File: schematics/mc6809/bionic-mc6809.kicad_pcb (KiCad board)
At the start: 2 copper layers, 48.3 x 71.1 mm, 12 parts, among them J1 Bionic-P135, J1 BionicConnector, J2 Bionic-P245, U1 MC6809P, U2 74HCT126, U3 11AA010-I/TO

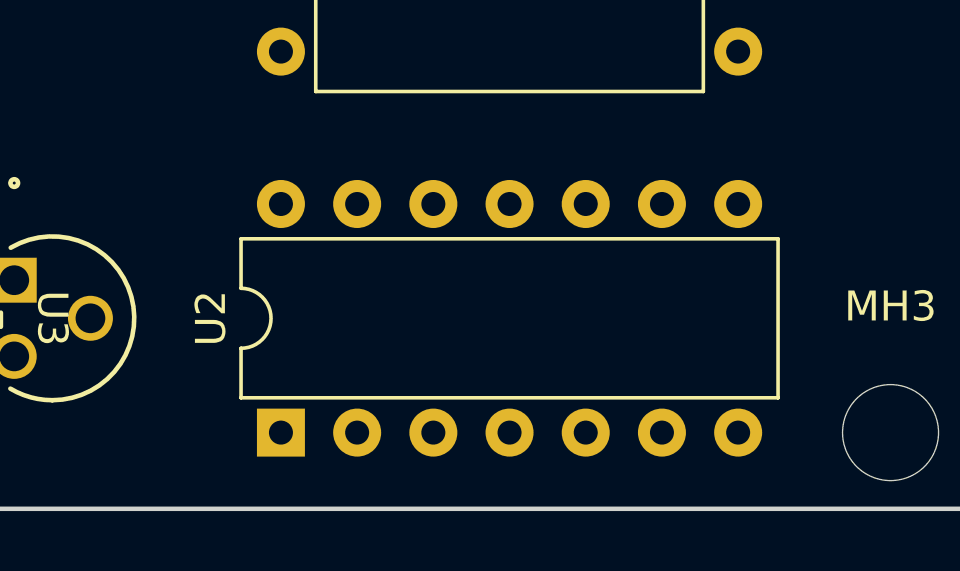
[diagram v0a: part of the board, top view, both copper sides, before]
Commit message: [MC6809] Remove HC126
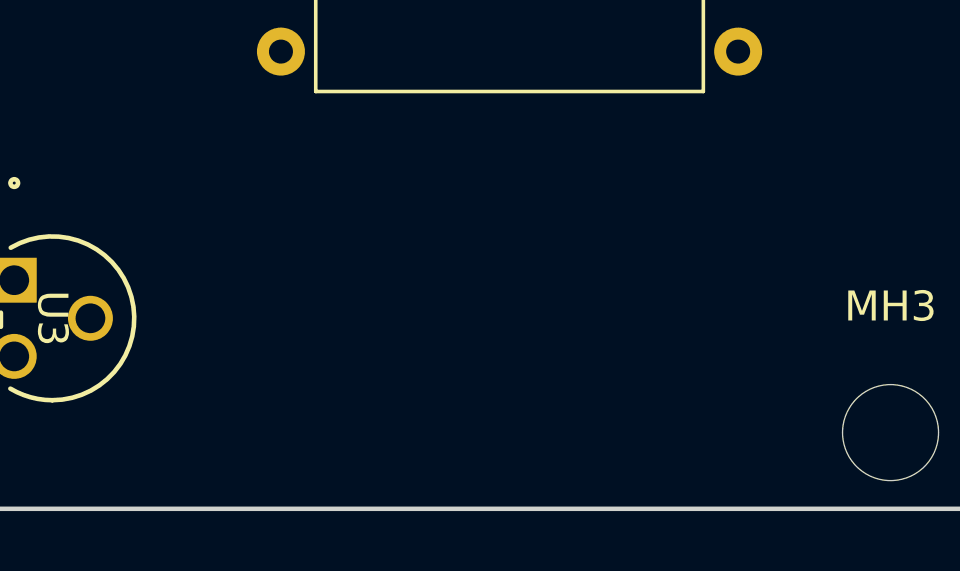
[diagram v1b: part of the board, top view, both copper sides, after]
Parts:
- removed U2: 74HCT126, Package_DIP:DIP-14_W7.62mm
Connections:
- U1 pad 37: Net-(U1-~{RESET}) -> /P53
- U1 pad 38: /EXTAL -> /P46
